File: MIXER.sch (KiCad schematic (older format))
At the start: 24 parts, among them K1 FRT5, U5 FST3253

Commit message: rotators 2 74lvc1G74
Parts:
- L10: value L_Small -> 33uH; footprint (none) -> Choke_Axial_ThroughHole:Choke_Horizontal_RM10mm
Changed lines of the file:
@@
 $EndComp
 $Comp
-L GND #PWR068
+L GND #PWR72
 U 1 1 5EA97A71
 P 8800 4950
-F 0 "#PWR068" H 8800 4700 50  0001 C CNN
+F 0 "#PWR72" H 8800 4700 50  0001 C CNN
 F 1 "GND" H 8800 4800 50  0001 C CNN
 F 2 "" H 8800 4950 50  0001 C CNN
@@
 $EndComp
 $Comp
-L GND #PWR069
+L GND #PWR71
 U 1 1 5EA97AA1
 P 8800 4350
-F 0 "#PWR069" H 8800 4100 50  0001 C CNN
+F 0 "#PWR71" H 8800 4100 50  0001 C CNN
 F 1 "GND" H 8800 4200 50  0001 C CNN
 F 2 "" H 8800 4350 50  0001 C CNN
@@
 $EndComp
 $Comp
-L GND #PWR070
+L GND #PWR70
 U 1 1 5EA97F13
 P 8800 3850
-F 0 "#PWR070" H 8800 3600 50  0001 C CNN
+F 0 "#PWR70" H 8800 3600 50  0001 C CNN
 F 1 "GND" H 8800 3700 50  0001 C CNN
 F 2 "" H 8800 3850 50  0001 C CNN
@@
 $EndComp
 $Comp
-L GND #PWR071
+L GND #PWR67
 U 1 1 5EA97F19
 P 6350 4950
-F 0 "#PWR071" H 6350 4700 50  0001 C CNN
+F 0 "#PWR67" H 6350 4700 50  0001 C CNN
 F 1 "GND" H 6350 4800 50  0001 C CNN
 F 2 "" H 6350 4950 50  0001 C CNN
@@
 $EndComp
 $Comp
-L GND #PWR072
+L GND #PWR69
 U 1 1 5EA994E9
 P 6850 3500
-F 0 "#PWR072" H 6850 3250 50  0001 C CNN
+F 0 "#PWR69" H 6850 3250 50  0001 C CNN
 F 1 "GND" H 6850 3350 50  0001 C CNN
 F 2 "" H 6850 3500 50  0001 C CNN
@@
 $EndComp
 $Comp
-L GND #PWR073
+L GND #PWR68
 U 1 1 5EA99527
 P 6650 3500
-F 0 "#PWR073" H 6650 3250 50  0001 C CNN
+F 0 "#PWR68" H 6650 3250 50  0001 C CNN
 F 1 "GND" H 6650 3350 50  0001 C CNN
 F 2 "" H 6650 3500 50  0001 C CNN
@@
 P 6850 2900
 F 0 "L10" H 6880 2940 50  0000 L CNN
-F 1 "L_Small" H 6880 2860 50  0000 L CNN
-F 2 "" H 6850 2900 50  0001 C CNN
+F 1 "33uH" H 6880 2860 50  0000 L CNN
+F 2 "Choke_Axial_ThroughHole:Choke_Horizontal_RM10mm" H 6850 2900 50  0001 C CNN
 F 3 "" H 6850 2900 50  0001 C CNN
 	1    6850 2900
@@
 	1450 3000 1050 3000
 $Comp
-L GND #PWR074
+L GND #PWR63
 U 1 1 5EAF8000
 P 1400 2650
-F 0 "#PWR074" H 1400 2400 50  0001 C CNN
+F 0 "#PWR63" H 1400 2400 50  0001 C CNN
 F 1 "GND" H 1400 2500 50  0001 C CNN
 F 2 "" H 1400 2650 50  0001 C CNN
@@
 $EndComp
 $Comp
-L GND #PWR075
+L GND #PWR73
 U 1 1 5EAFBA4D
 P 8800 5500
-F 0 "#PWR075" H 8800 5250 50  0001 C CNN
+F 0 "#PWR73" H 8800 5250 50  0001 C CNN
 F 1 "GND" H 8800 5350 50  0001 C CNN
 F 2 "" H 8800 5500 50  0001 C CNN
@@
 	5350 3600 5350 4350
 $Comp
-L GND #PWR076
+L GND #PWR66
 U 1 1 5EB03067
 P 5350 4550
-F 0 "#PWR076" H 5350 4300 50  0001 C CNN
+F 0 "#PWR66" H 5350 4300 50  0001 C CNN
 F 1 "GND" H 5350 4400 50  0001 C CNN
 F 2 "" H 5350 4550 50  0001 C CNN
@@
 $EndComp
 $Comp
-L GND #PWR077
+L GND #PWR65
 U 1 1 5EB039FD
 P 5000 4550
-F 0 "#PWR077" H 5000 4300 50  0001 C CNN
+F 0 "#PWR65" H 5000 4300 50  0001 C CNN
 F 1 "GND" H 5000 4400 50  0001 C CNN
 F 2 "" H 5000 4550 50  0001 C CNN
@@
 $EndComp
 $Comp
-L GND #PWR078
+L GND #PWR64
 U 1 1 5EB03A50
 P 4750 4550
-F 0 "#PWR078" H 4750 4300 50  0001 C CNN
+F 0 "#PWR64" H 4750 4300 50  0001 C CNN
 F 1 "GND" H 4750 4400 50  0001 C CNN
 F 2 "" H 4750 4550 50  0001 C CNN

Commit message: PCB s1
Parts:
- removed K1: FRT5, Relays_THT:Relay_DPDT_FRT5, symbol FRT5
- removed U5: FST3253, Housings_SSOP:TSSOP-16_4.4x5mm_Pitch0.65mm, symbol FST3253
- added U5, U7: FSA3157, TO_SOT_Packages_SMD:SOT-363_SC-70-6, symbol NC7SB3157
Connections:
- wire segments 69 -> 47
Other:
- moved on the sheet: C81, C82, C83, C84, C85, C86, C87, C88, R3, R4, R66, R7

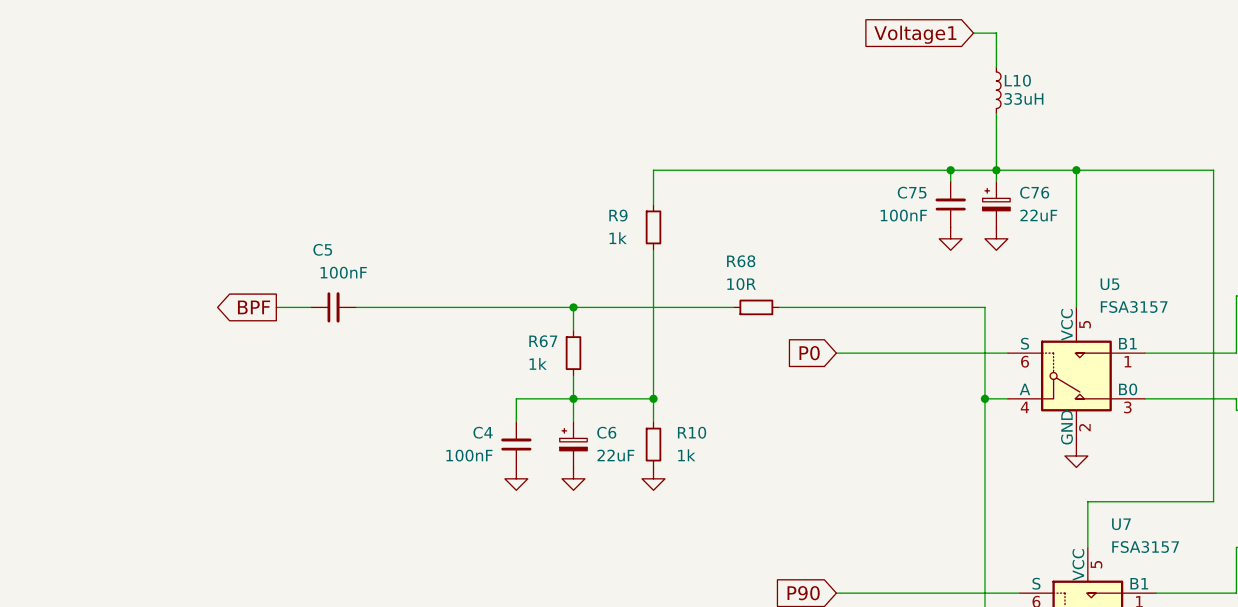
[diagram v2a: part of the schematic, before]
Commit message: need some GND vias
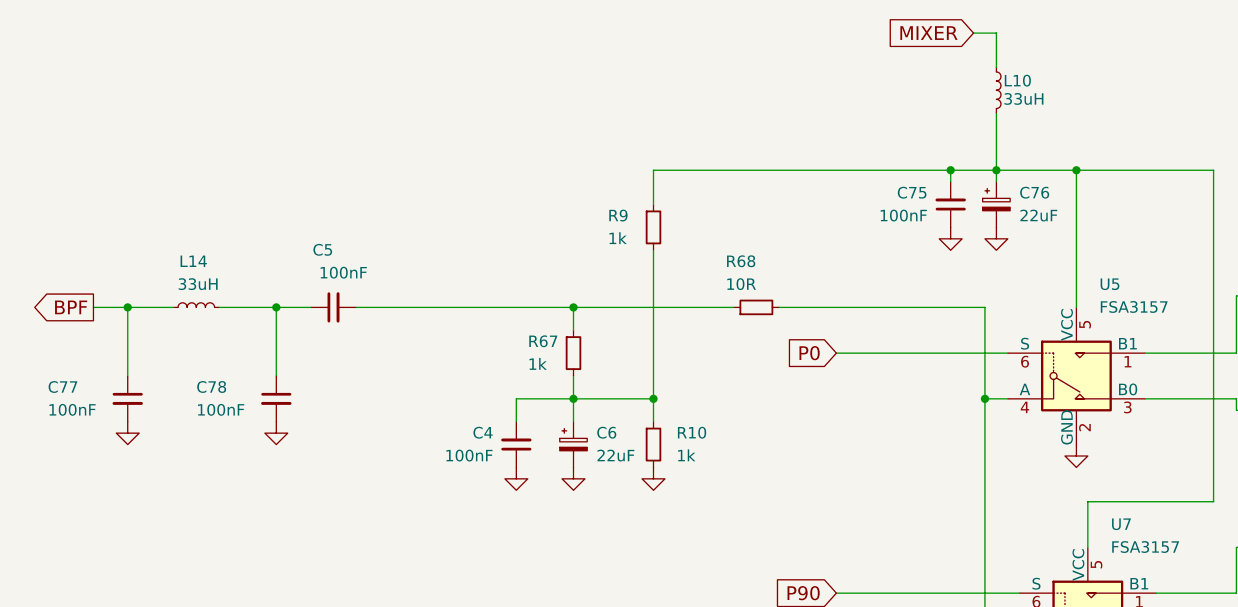
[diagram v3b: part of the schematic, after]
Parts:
- added C77, C78: 100nF, Capacitors_THT:C_Disc_D7.0mm_W2.5mm_P5.00mm, symbol C_Small
- added L14: 33uH, Choke_Axial_ThroughHole:Choke_Horizontal_RM10mm, symbol L_Small
- C5: footprint UI:C_1206_0603 -> Capacitors_THT:C_Disc_D7.0mm_W2.5mm_P5.00mm
- C6, C76: footprint Capacitors_Tantalum_SMD:CP_Tantalum_Case-A_EIA-3216-18_Wave -> Capacitors_THT:CP_Radial_D5.0mm_P2.00mm
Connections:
- net BPF: now also C77.1, L14.1; no longer C5.1
- net GND: now also C77.2, C78.2
- net Voltage1 renamed MIXER
- new net: C5.1, C78.1, L14.2
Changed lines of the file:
@@
 $Descr A4 11693 8268
 encoding utf-8
-Sheet 8 8
+Sheet 8 7
 Title ""
 Date ""
@@
 $EndComp
 $Comp
-L GND #PWR063
+L GND #PWR091
 U 1 1 5EA97A71
 P 8800 5150
-F 0 "#PWR063" H 8800 4900 50  0001 C CNN
+F 0 "#PWR091" H 8800 4900 50  0001 C CNN
 F 1 "GND" H 8800 5000 50  0001 C CNN
 F 2 "" H 8800 5150 50  0001 C CNN
@@
 $EndComp
 $Comp
-L GND #PWR064
+L GND #PWR092
 U 1 1 5EA97AA1
 P 8800 4550
-F 0 "#PWR064" H 8800 4300 50  0001 C CNN
+F 0 "#PWR092" H 8800 4300 50  0001 C CNN
 F 1 "GND" H 8800 4400 50  0001 C CNN
 F 2 "" H 8800 4550 50  0001 C CNN
@@
 $EndComp
 $Comp
-L GND #PWR065
+L GND #PWR093
 U 1 1 5EA97F13
 P 8800 4050
-F 0 "#PWR065" H 8800 3800 50  0001 C CNN
+F 0 "#PWR093" H 8800 3800 50  0001 C CNN
 F 1 "GND" H 8800 3900 50  0001 C CNN
 F 2 "" H 8800 4050 50  0001 C CNN
@@
 $EndComp
 $Comp
-L GND #PWR066
+L GND #PWR094
 U 1 1 5EA97F19
 P 7200 4450
-F 0 "#PWR066" H 7200 4200 50  0001 C CNN
+F 0 "#PWR094" H 7200 4200 50  0001 C CNN
 F 1 "GND" H 7200 4300 50  0001 C CNN
 F 2 "" H 7200 4450 50  0001 C CNN
@@
 F 0 "C76" H 6950 3450 50  0000 L CNN
 F 1 "22uF" H 6950 3350 50  0000 L CNN
-F 2 "Capacitors_Tantalum_SMD:CP_Tantalum_Case-A_EIA-3216-18_Wave" H 6850 3400 50  0001 C CNN
+F 2 "Capacitors_THT:CP_Radial_D5.0mm_P2.00mm" H 6850 3400 50  0001 C CNN
 F 3 "" H 6850 3400 50  0001 C CNN
 	1    6850 3400
@@
 $EndComp
 $Comp
-L GND #PWR067
+L GND #PWR095
 U 1 1 5EA994E9
 P 6850 3500
-F 0 "#PWR067" H 6850 3250 50  0001 C CNN
+F 0 "#PWR095" H 6850 3250 50  0001 C CNN
 F 1 "GND" H 6850 3350 50  0001 C CNN
 F 2 "" H 6850 3500 50  0001 C CNN
@@
 $EndComp
 $Comp
-L GND #PWR068
+L GND #PWR096
 U 1 1 5EA99527
 P 6650 3500
-F 0 "#PWR068" H 6650 3250 50  0001 C CNN
+F 0 "#PWR096" H 6650 3250 50  0001 C CNN
 F 1 "GND" H 6650 3350 50  0001 C CNN
 F 2 "" H 6650 3500 50  0001 C CNN
@@
 $EndComp
 $Comp
-L GND #PWR069
+L GND #PWR097
 U 1 1 5EAFBA4D
 P 8800 5700
-F 0 "#PWR069" H 8800 5450 50  0001 C CNN
+F 0 "#PWR097" H 8800 5450 50  0001 C CNN
 F 1 "GND" H 8800 5550 50  0001 C CNN
 F 2 "" H 8800 5700 50  0001 C CNN
@@
 	6650 3300 6650 3250
 Connection ~ 6650 3250
-Wire Wire Line
-	3700 3850 3850 3850
 $Comp
 L C_Small C5
@@
 F 0 "C5" V 4200 3850 50  0000 L CNN
 F 1 "100nF" V 4100 3700 50  0000 L CNN
-F 2 "UI:C_1206_0603" H 3950 3850 50  0001 C CNN
+F 2 "Capacitors_THT:C_Disc_D7.0mm_W2.5mm_P5.00mm" H 3950 3850 50  0001 C CNN
 F 3 "" H 3950 3850 50  0001 C CNN
 	1    3950 3850
@@
 Wire Wire Line
 	4050 3850 5700 3850
-Text GLabel 3700 3850 0    60   Output ~ 0
+Text GLabel 2900 3850 0    60   Output ~ 0
 BPF
 Text GLabel 6750 2650 0    60   Input ~ 0
-Voltage1
+MIXER
 Wire Wire Line
 	6750 2650 6850 2650
@@
 	5350 3600 5350 4350
 $Comp
-L GND #PWR070
+L GND #PWR098
 U 1 1 5EB03067
 P 5350 4550
-F 0 "#PWR070" H 5350 4300 50  0001 C CNN
+F 0 "#PWR098" H 5350 4300 50  0001 C CNN
 F 1 "GND" H 5350 4400 50  0001 C CNN
 F 2 "" H 5350 4550 50  0001 C CNN
@@
 F 0 "C6" H 5100 4500 50  0000 L CNN
 F 1 "22uF" H 5100 4400 50  0000 L CNN
-F 2 "Capacitors_Tantalum_SMD:CP_Tantalum_Case-A_EIA-3216-18_Wave" H 5000 4450 50  0001 C CNN
+F 2 "Capacitors_THT:CP_Radial_D5.0mm_P2.00mm" H 5000 4450 50  0001 C CNN
 F 3 "" H 5000 4450 50  0001 C CNN
 	1    5000 4450
@@
 $EndComp
 $Comp
-L GND #PWR071
+L GND #PWR099
 U 1 1 5EB039FD
 P 5000 4550
-F 0 "#PWR071" H 5000 4300 50  0001 C CNN
+F 0 "#PWR099" H 5000 4300 50  0001 C CNN
 F 1 "GND" H 5000 4400 50  0001 C CNN
 F 2 "" H 5000 4550 50  0001 C CNN
@@
 $EndComp
 $Comp
-L GND #PWR072
+L GND #PWR0100
 U 1 1 5EB03A50
 P 4750 4550
-F 0 "#PWR072" H 4750 4300 50  0001 C CNN
+F 0 "#PWR0100" H 4750 4300 50  0001 C CNN
 F 1 "GND" H 4750 4400 50  0001 C CNN
 F 2 "" H 4750 4550 50  0001 C CNN
@@
 $EndComp
 Wire Wire Line
-	7200 3850 7200 3250
+	7200 3250 7200 3850
 Wire Wire Line
 	5350 3250 7800 3250
@@
 	7900 5300 7900 5450
 $Comp
-L GND #PWR073
+L GND #PWR0101
 U 1 1 5EB0FF22
 P 7250 5500
-F 0 "#PWR073" H 7250 5250 50  0001 C CNN
+F 0 "#PWR0101" H 7250 5250 50  0001 C CNN
 F 1 "GND" H 7250 5350 50  0001 C CNN
 F 2 "" H 7250 5500 50  0001 C CNN
@@
 	6900 4250 6800 4250
 Connection ~ 6800 4250
+$Comp
+L L_Small L14
+U 1 1 5EBC2D6F
+P 3350 3850
+F 0 "L14" V 3550 3800 50  0000 L CNN
+F 1 "33uH" V 3450 3750 50  0000 L CNN
+F 2 "Choke_Axial_ThroughHole:Choke_Horizontal_RM10mm" H 3350 3850 50  0001 C CNN
+F 3 "" H 3350 3850 50  0001 C CNN
+	1    3350 3850
+	0    -1   -1   0
+$EndComp
+$Comp
+L C_Small C77
+U 1 1 5EBC2FB8
+P 3050 4250
+F 0 "C77" H 2700 4300 50  0000 L CNN
+F 1 "100nF" H 2700 4200 50  0000 L CNN
+F 2 "Capacitors_THT:C_Disc_D7.0mm_W2.5mm_P5.00mm" H 3050 4250 50  0001 C CNN
+F 3 "" H 3050 4250 50  0001 C CNN
+	1    3050 4250
+	1    0    0    -1
+$EndComp
+Wire Wire Line
+	2900 3850 3250 3850
+Wire Wire Line
+	3450 3850 3850 3850
+Wire Wire Line
+	3050 4150 3050 3850
+Connection ~ 3050 3850
+$Comp
+L GND #PWR0102
+U 1 1 5EBC3390
+P 3050 4350
+F 0 "#PWR0102" H 3050 4100 50  0001 C CNN
+F 1 "GND" H 3050 4200 50  0001 C CNN
+F 2 "" H 3050 4350 50  0001 C CNN
+F 3 "" H 3050 4350 50  0001 C CNN
+	1    3050 4350
+	1    0    0    -1
+$EndComp
+$Comp
+L C_Small C78
+U 1 1 5EBC3A55
+P 3700 4250
+F 0 "C78" H 3350 4300 50  0000 L CNN
+F 1 "100nF" H 3350 4200 50  0000 L CNN
+F 2 "Capacitors_THT:C_Disc_D7.0mm_W2.5mm_P5.00mm" H 3700 4250 50  0001 C CNN
+F 3 "" H 3700 4250 50  0001 C CNN
+	1    3700 4250
+	1    0    0    -1
+$EndComp
+$Comp
+L GND #PWR0103
+U 1 1 5EBC3AC8
+P 3700 4350
+F 0 "#PWR0103" H 3700 4100 50  0001 C CNN
+F 1 "GND" H 3700 4200 50  0001 C CNN
+F 2 "" H 3700 4350 50  0001 C CNN
+F 3 "" H 3700 4350 50  0001 C CNN
+	1    3700 4350
+	1    0    0    -1
+$EndComp
+Wire Wire Line
+	3700 4150 3700 3850
+Connection ~ 3700 3850
 $EndSCHEMATC

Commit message: Phase shift with 74LCX574 TSSOP-20
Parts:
- U5, U7: footprint TO_SOT_Packages_SMD:SOT-363_SC-70-6 -> TO_SOT_Packages_SMD:SOT-23-6
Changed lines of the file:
@@
 $EndComp
 $Comp
-L GND #PWR091
+L GND #PWR092
 U 1 1 5EA97A71
 P 8800 5150
-F 0 "#PWR091" H 8800 4900 50  0001 C CNN
+F 0 "#PWR092" H 8800 4900 50  0001 C CNN
 F 1 "GND" H 8800 5000 50  0001 C CNN
 F 2 "" H 8800 5150 50  0001 C CNN
@@
 $EndComp
 $Comp
-L GND #PWR092
+L GND #PWR093
 U 1 1 5EA97AA1
 P 8800 4550
-F 0 "#PWR092" H 8800 4300 50  0001 C CNN
+F 0 "#PWR093" H 8800 4300 50  0001 C CNN
 F 1 "GND" H 8800 4400 50  0001 C CNN
 F 2 "" H 8800 4550 50  0001 C CNN
@@
 $EndComp
 $Comp
-L GND #PWR093
+L GND #PWR094
 U 1 1 5EA97F13
 P 8800 4050
-F 0 "#PWR093" H 8800 3800 50  0001 C CNN
+F 0 "#PWR094" H 8800 3800 50  0001 C CNN
 F 1 "GND" H 8800 3900 50  0001 C CNN
 F 2 "" H 8800 4050 50  0001 C CNN
@@
 $EndComp
 $Comp
-L GND #PWR094
+L GND #PWR095
 U 1 1 5EA97F19
 P 7200 4450
-F 0 "#PWR094" H 7200 4200 50  0001 C CNN
+F 0 "#PWR095" H 7200 4200 50  0001 C CNN
 F 1 "GND" H 7200 4300 50  0001 C CNN
 F 2 "" H 7200 4450 50  0001 C CNN
@@
 $EndComp
 $Comp
-L GND #PWR095
+L GND #PWR096
 U 1 1 5EA994E9
 P 6850 3500
-F 0 "#PWR095" H 6850 3250 50  0001 C CNN
+F 0 "#PWR096" H 6850 3250 50  0001 C CNN
 F 1 "GND" H 6850 3350 50  0001 C CNN
 F 2 "" H 6850 3500 50  0001 C CNN
@@
 $EndComp
 $Comp
-L GND #PWR096
+L GND #PWR097
 U 1 1 5EA99527
 P 6650 3500
-F 0 "#PWR096" H 6650 3250 50  0001 C CNN
+F 0 "#PWR097" H 6650 3250 50  0001 C CNN
 F 1 "GND" H 6650 3350 50  0001 C CNN
 F 2 "" H 6650 3500 50  0001 C CNN
@@
 $EndComp
 $Comp
-L GND #PWR097
+L GND #PWR098
 U 1 1 5EAFBA4D
 P 8800 5700
-F 0 "#PWR097" H 8800 5450 50  0001 C CNN
+F 0 "#PWR098" H 8800 5450 50  0001 C CNN
 F 1 "GND" H 8800 5550 50  0001 C CNN
 F 2 "" H 8800 5700 50  0001 C CNN
@@
 	5350 3600 5350 4350
 $Comp
-L GND #PWR098
+L GND #PWR099
 U 1 1 5EB03067
 P 5350 4550
-F 0 "#PWR098" H 5350 4300 50  0001 C CNN
+F 0 "#PWR099" H 5350 4300 50  0001 C CNN
 F 1 "GND" H 5350 4400 50  0001 C CNN
 F 2 "" H 5350 4550 50  0001 C CNN
@@
 $EndComp
 $Comp
-L GND #PWR099
+L GND #PWR0100
 U 1 1 5EB039FD
 P 5000 4550
-F 0 "#PWR099" H 5000 4300 50  0001 C CNN
+F 0 "#PWR0100" H 5000 4300 50  0001 C CNN
 F 1 "GND" H 5000 4400 50  0001 C CNN
 F 2 "" H 5000 4550 50  0001 C CNN
@@
 $EndComp
 $Comp
-L GND #PWR0100
+L GND #PWR0101
 U 1 1 5EB03A50
 P 4750 4550
-F 0 "#PWR0100" H 4750 4300 50  0001 C CNN
+F 0 "#PWR0101" H 4750 4300 50  0001 C CNN
 F 1 "GND" H 4750 4400 50  0001 C CNN
 F 2 "" H 4750 4550 50  0001 C CNN
@@
 F 0 "U5" H 7300 4550 50  0000 L CNN
 F 1 "FSA3157" H 7300 4450 50  0000 L CNN
-F 2 "TO_SOT_Packages_SMD:SOT-363_SC-70-6" H 7200 4200 50  0001 C CNN
+F 2 "TO_SOT_Packages_SMD:SOT-23-6" H 7200 4200 50  0001 C CNN
 F 3 "" H 7200 4200 50  0001 C CNN
 	1    7200 4150
@@
 F 0 "U7" H 7350 5600 50  0000 L CNN
 F 1 "FSA3157" H 7350 5500 50  0000 L CNN
-F 2 "TO_SOT_Packages_SMD:SOT-363_SC-70-6" H 7250 5250 50  0001 C CNN
+F 2 "TO_SOT_Packages_SMD:SOT-23-6" H 7250 5250 50  0001 C CNN
 F 3 "" H 7250 5250 50  0001 C CNN
 	1    7250 5200
@@
 	7900 5300 7900 5450
 $Comp
-L GND #PWR0101
+L GND #PWR0102
 U 1 1 5EB0FF22
 P 7250 5500
-F 0 "#PWR0101" H 7250 5250 50  0001 C CNN
+F 0 "#PWR0102" H 7250 5250 50  0001 C CNN
 F 1 "GND" H 7250 5350 50  0001 C CNN
 F 2 "" H 7250 5500 50  0001 C CNN
@@
 Connection ~ 3050 3850
 $Comp
-L GND #PWR0102
+L GND #PWR0103
 U 1 1 5EBC3390
 P 3050 4350
-F 0 "#PWR0102" H 3050 4100 50  0001 C CNN
+F 0 "#PWR0103" H 3050 4100 50  0001 C CNN
 F 1 "GND" H 3050 4200 50  0001 C CNN
 F 2 "" H 3050 4350 50  0001 C CNN
@@
 $EndComp
 $Comp
-L GND #PWR0103
+L GND #PWR0104
 U 1 1 5EBC3AC8
 P 3700 4350
-F 0 "#PWR0103" H 3700 4100 50  0001 C CNN
+F 0 "#PWR0104" H 3700 4100 50  0001 C CNN
 F 1 "GND" H 3700 4200 50  0001 C CNN
 F 2 "" H 3700 4350 50  0001 C CNN
